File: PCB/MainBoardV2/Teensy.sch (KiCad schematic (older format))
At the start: 44 parts, among them Q5 NTR4003NT3G, Q6 NTR4003NT3G, Q7 NTR4003NT3G, Q8 NTR4003NT3G, Q9 NTR4003NT3G, SW3 PTS645SM43SMTR92 LFS, U5 Teensy3.6

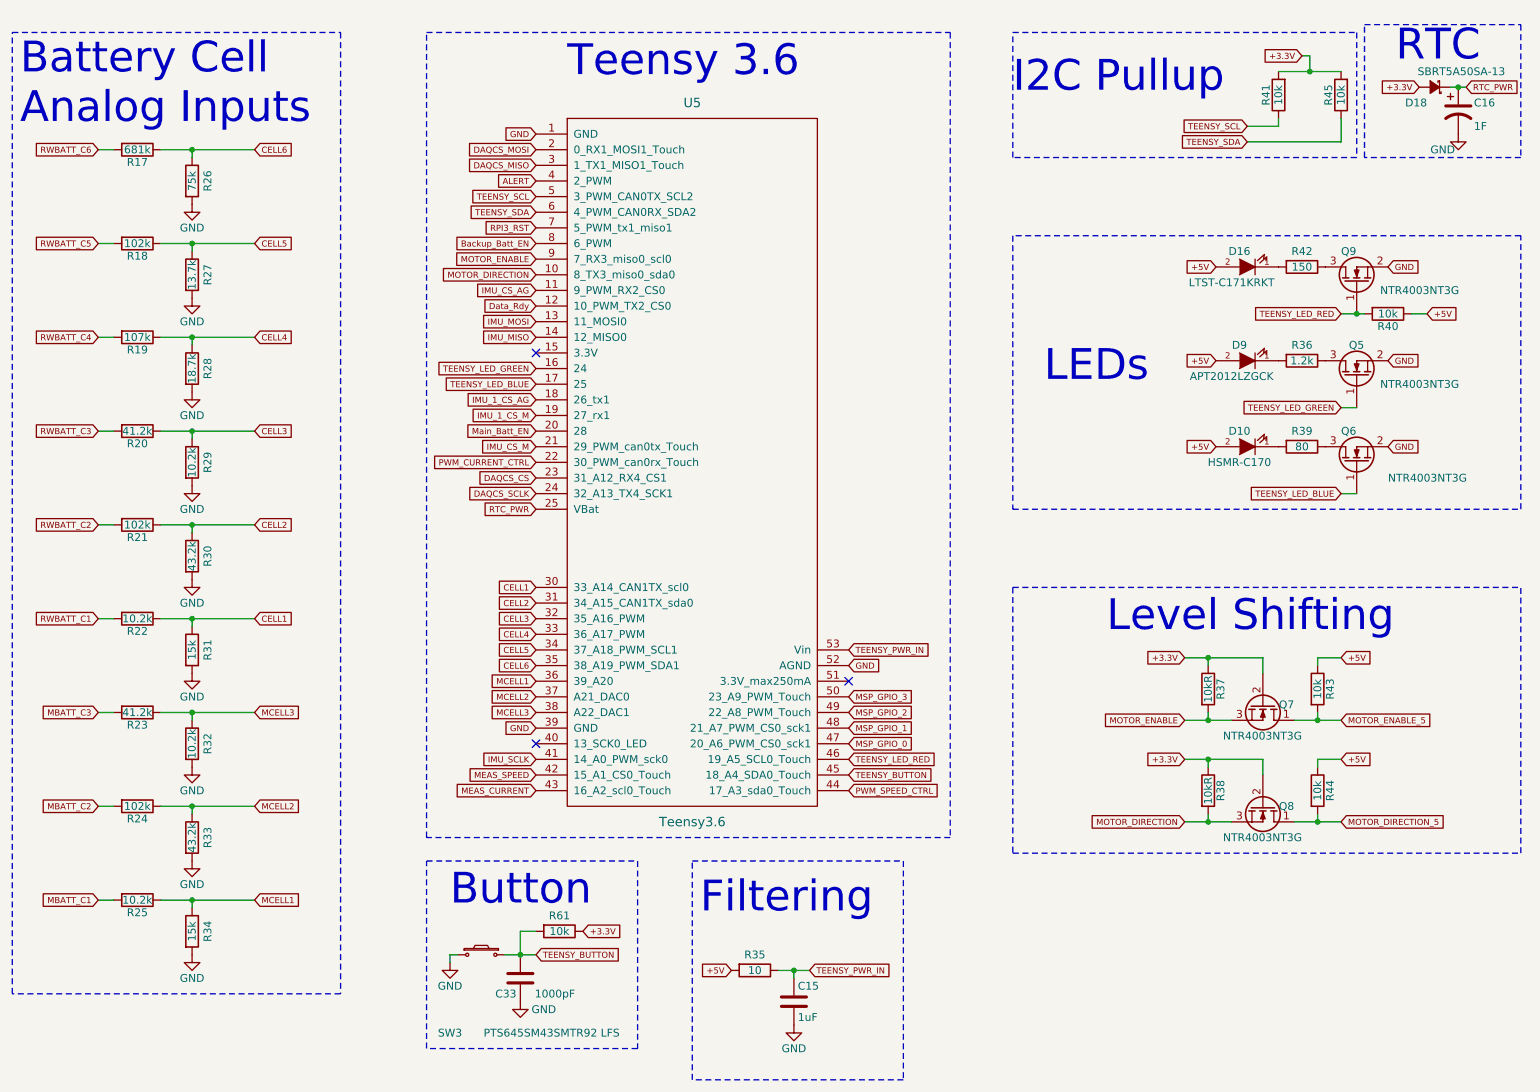
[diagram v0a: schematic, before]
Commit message: Layout Done - Needs TPs Still
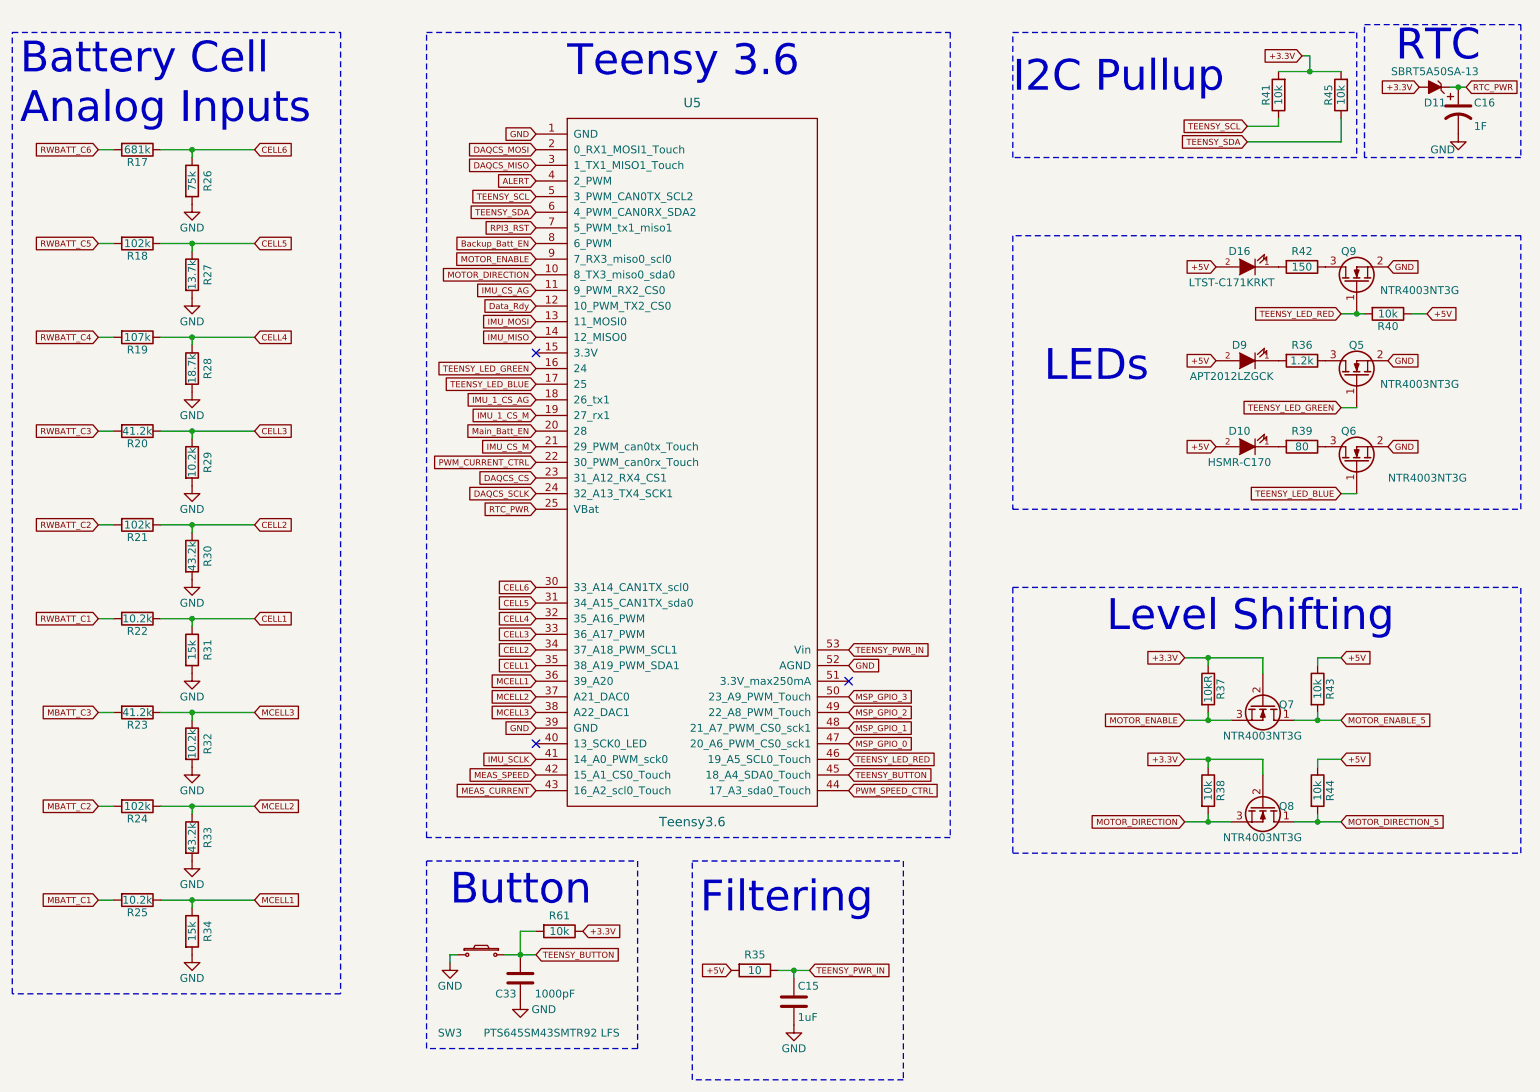
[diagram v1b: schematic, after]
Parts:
- removed D18: SBRT5A50SA-13, Dans_Parts:DO-214AC_Schottky, symbol D_Schottky_Small
- added D11: SBRT5A50SA-13, Dans_Parts:DO-214AC_Schottky, symbol ZENERsmall
- R38: value 10kR -> 10k
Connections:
- net +3.3V: now also D11.1 (A)
- net CELL1: now also U5.35 (38_A19_PWM_SDA1); no longer U5.30 (33_A14_CAN1TX_scl0)
- net CELL2: now also U5.34 (37_A18_PWM_SCL1); no longer U5.31 (34_A15_CAN1TX_sda0)
- net CELL3: now also U5.33 (36_A17_PWM); no longer U5.32 (35_A16_PWM)
- net CELL4: now also U5.32 (35_A16_PWM); no longer U5.33 (36_A17_PWM)
- net CELL5: now also U5.31 (34_A15_CAN1TX_sda0); no longer U5.34 (37_A18_PWM_SCL1)
- net CELL6: now also U5.30 (33_A14_CAN1TX_scl0); no longer U5.35 (38_A19_PWM_SDA1)
- net RTC_PWR: now also D11.2 (K)
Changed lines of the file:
@@
 	2100 4750 2700 4750
 $Comp
-L GND #PWR52
+L GND #PWR048
 U 1 1 5A0B49DD
 P 2300 5100
-F 0 "#PWR52" H 2300 4850 50  0001 C CNN
+F 0 "#PWR048" H 2300 4850 50  0001 C CNN
 F 1 "GND" H 2300 4950 50  0000 C CNN
 F 2 "" H 2300 5100 50  0000 C CNN
@@
 	2100 4150 2700 4150
 $Comp
-L GND #PWR51
+L GND #PWR049
 U 1 1 5A0B6A32
 P 2300 4500
-F 0 "#PWR51" H 2300 4250 50  0001 C CNN
+F 0 "#PWR049" H 2300 4250 50  0001 C CNN
 F 1 "GND" H 2300 4350 50  0000 C CNN
 F 2 "" H 2300 4500 50  0000 C CNN
@@
 	2100 3550 2700 3550
 $Comp
-L GND #PWR50
+L GND #PWR050
 U 1 1 5A0B6B68
 P 2300 3900
-F 0 "#PWR50" H 2300 3650 50  0001 C CNN
+F 0 "#PWR050" H 2300 3650 50  0001 C CNN
 F 1 "GND" H 2300 3750 50  0000 C CNN
 F 2 "" H 2300 3900 50  0000 C CNN
@@
 	2100 2950 2700 2950
 $Comp
-L GND #PWR49
+L GND #PWR051
 U 1 1 5A0B6D35
 P 2300 3300
-F 0 "#PWR49" H 2300 3050 50  0001 C CNN
+F 0 "#PWR051" H 2300 3050 50  0001 C CNN
 F 1 "GND" H 2300 3150 50  0000 C CNN
 F 2 "" H 2300 3300 50  0000 C CNN
@@
 	2100 2350 2700 2350
 $Comp
-L GND #PWR48
+L GND #PWR052
 U 1 1 5A0B6F82
 P 2300 2700
-F 0 "#PWR48" H 2300 2450 50  0001 C CNN
+F 0 "#PWR052" H 2300 2450 50  0001 C CNN
 F 1 "GND" H 2300 2550 50  0000 C CNN
 F 2 "" H 2300 2700 50  0000 C CNN
@@
 	2100 1750 2700 1750
 $Comp
-L GND #PWR47
+L GND #PWR053
 U 1 1 5A0B7025
 P 2300 2100
-F 0 "#PWR47" H 2300 1850 50  0001 C CNN
+F 0 "#PWR053" H 2300 1850 50  0001 C CNN
 F 1 "GND" H 2300 1950 50  0000 C CNN
 F 2 "" H 2300 2100 50  0000 C CNN
@@
 Text GLabel 2700 1750 2    39   Input ~ 0
 CELL6
+Text GLabel 4500 5050 0    39   Input ~ 0
+CELL1
+Text GLabel 4500 4950 0    39   Input ~ 0
+CELL2
+Text GLabel 4500 4850 0    39   Input ~ 0
+CELL3
+Text GLabel 4500 4750 0    39   Input ~ 0
+CELL4
+Text GLabel 4500 4650 0    39   Input ~ 0
+CELL5
 Text GLabel 4500 4550 0    39   Input ~ 0
-CELL1
-Text GLabel 4500 4650 0    39   Input ~ 0
-CELL2
-Text GLabel 4500 4750 0    39   Input ~ 0
-CELL3
-Text GLabel 4500 4850 0    39   Input ~ 0
-CELL4
-Text GLabel 4500 4950 0    39   Input ~ 0
-CELL5
-Text GLabel 4500 5050 0    39   Input ~ 0
 CELL6
 Text Notes 1200 1600 0    197  ~ 0
@@
 	2100 6550 2700 6550
 $Comp
-L GND #PWR55
+L GND #PWR054
 U 1 1 5A370907
 P 2300 6900
-F 0 "#PWR55" H 2300 6650 50  0001 C CNN
+F 0 "#PWR054" H 2300 6650 50  0001 C CNN
 F 1 "GND" H 2300 6750 50  0000 C CNN
 F 2 "" H 2300 6900 50  0000 C CNN
@@
 	2100 5950 2700 5950
 $Comp
-L GND #PWR54
+L GND #PWR055
 U 1 1 5A37092C
 P 2300 6300
-F 0 "#PWR54" H 2300 6050 50  0001 C CNN
+F 0 "#PWR055" H 2300 6050 50  0001 C CNN
 F 1 "GND" H 2300 6150 50  0000 C CNN
 F 2 "" H 2300 6300 50  0000 C CNN
@@
 	2100 5350 2700 5350
 $Comp
-L GND #PWR53
+L GND #PWR056
 U 1 1 5A370951
 P 2300 5700
-F 0 "#PWR53" H 2300 5450 50  0001 C CNN
+F 0 "#PWR056" H 2300 5450 50  0001 C CNN
 F 1 "GND" H 2300 5550 50  0000 C CNN
 F 2 "" H 2300 5700 50  0000 C CNN
@@
 P 8800 5850
 F 0 "R38" V 8880 5850 50  0000 C CNN
-F 1 "10kR" V 8800 5850 50  0000 C CNN
+F 1 "10k" V 8800 5850 50  0000 C CNN
 F 2 "Resistors_SMD:R_0805_HandSoldering" V 8730 5850 50  0001 C CNN
 F 3 "" H 8800 5850 50  0000 C CNN
@@
 Connection ~ 9500 6050
 $Comp
-L GND #PWR59
+L GND #PWR057
 U 1 1 5A4DF293
 P 10400 1650
-F 0 "#PWR59" H 10400 1400 50  0001 C CNN
+F 0 "#PWR057" H 10400 1400 50  0001 C CNN
 F 1 "GND" H 10300 1550 50  0000 C CNN
 F 2 "" H 10400 1650 50  0000 C CNN
@@
 	1    10400 1650
 	1    0    0    -1
-$EndComp
-$Comp
-L D_Schottky_Small D18
-U 1 1 5A4DF299
-P 10250 1350
-F 0 "D18" H 10300 1450 50  0000 L CNN
-F 1 "SBRT5A50SA-13" H 9800 1250 50  0000 L CNN
-F 2 "Dans_Parts:DO-214AC_Schottky" V 10250 1350 50  0001 C CNN
-F 3 "" V 10250 1350 50  0000 C CNN
-	1    10250 1350
-	-1   0    0    1
 $EndComp
 Text GLabel 10150 1350 0    39   Input ~ 0
@@
 RTC_PWR
 $Comp
-L GND #PWR58
+L GND #PWR058
 U 1 1 5A706281
 P 6150 7350
-F 0 "#PWR58" H 6150 7100 50  0001 C CNN
+F 0 "#PWR058" H 6150 7100 50  0001 C CNN
 F 1 "GND" H 6150 7200 50  0000 C CNN
 F 2 "" H 6150 7350 50  0000 C CNN
@@
 $EndComp
 $Comp
-L GND #PWR56
+L GND #PWR059
 U 1 1 5A74B436
 P 3950 6950
-F 0 "#PWR56" H 3950 6700 50  0001 C CNN
+F 0 "#PWR059" H 3950 6700 50  0001 C CNN
 F 1 "GND" H 3950 6800 50  0000 C CNN
 F 2 "" H 3950 6950 50  0000 C CNN
@@
 $EndComp
 $Comp
-L GND #PWR57
+L GND #PWR060
 U 1 1 5A74B445
 P 4400 7200
-F 0 "#PWR57" H 4400 6950 50  0001 C CNN
+F 0 "#PWR060" H 4400 6950 50  0001 C CNN
 F 1 "GND" H 4550 7150 50  0000 C CNN
 F 2 "" H 4400 7200 50  0000 C CNN
@@
 Wire Wire Line
 	10100 2800 10200 2800
+$Comp
+L ZENERsmall D11
+U 1 1 5A7CB597
+P 10250 1350
+F 0 "D11" H 10250 1450 50  0000 C CNN
+F 1 "SBRT5A50SA-13" H 10250 1250 50  0000 C CNN
+F 2 "Dans_Parts:DO-214AC_Schottky" H 10250 1350 50  0001 C CNN
+F 3 "" H 10250 1350 50  0000 C CNN
+	1    10250 1350
+	-1   0    0    1
+$EndComp
 $EndSCHEMATC

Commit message: Added BOM, Couple Fixes, Couple Misc Documents
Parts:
- C33: value 1000pF -> 1nF
- D11: value SBRT5A50SA-13 -> CDBA540-HF
- R37: value 10kR -> 10k
- R39: value 80 -> 100
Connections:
- net +3.3V: now also R40.1
- net +5V: no longer R40.1
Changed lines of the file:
@@
 P 8800 5200
 F 0 "R37" V 8880 5200 50  0000 C CNN
-F 1 "10kR" V 8800 5200 50  0000 C CNN
+F 1 "10k" V 8800 5200 50  0000 C CNN
 F 2 "Resistors_SMD:R_0805_HandSoldering" V 8730 5200 50  0001 C CNN
 F 3 "" H 8800 5200 50  0000 C CNN
@@
 P 4400 7050
 F 0 "C33" H 4425 7150 50  0000 L CNN
-F 1 "1000pF" H 4050 7150 50  0000 L CNN
+F 1 "1nF" H 4200 7150 50  0000 L CNN
 F 2 "Capacitors_SMD:C_0805_HandSoldering" H 4438 6900 50  0001 C CNN
 F 3 "" H 4400 7050 50  0000 C CNN
@@
 P 9400 3650
 F 0 "R39" V 9300 3650 50  0000 C CNN
-F 1 "80" V 9400 3650 50  0000 C CNN
+F 1 "100" V 9400 3650 50  0000 C CNN
 F 2 "Resistors_SMD:R_0805_HandSoldering" V 9330 3650 50  0001 C CNN
 F 3 "" H 9400 3650 50  0000 C CNN
@@
 $EndComp
 Text GLabel 10200 2800 2    39   Input ~ 0
-+5V
++3.3V
 Connection ~ 9750 2800
 Wire Wire Line
@@
 P 10250 1350
 F 0 "D11" H 10250 1450 50  0000 C CNN
-F 1 "SBRT5A50SA-13" H 10250 1250 50  0000 C CNN
+F 1 "CDBA540-HF" H 10250 1250 50  0000 C CNN
 F 2 "Dans_Parts:DO-214AC_Schottky" H 10250 1350 50  0001 C CNN
 F 3 "" H 10250 1350 50  0000 C CNN
